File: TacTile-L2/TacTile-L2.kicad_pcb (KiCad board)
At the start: 2 copper layers, 21.2 x 60 mm, 11 parts, among them J1 Conn_01x05, J2 Conn_01x05, U1 74HC595

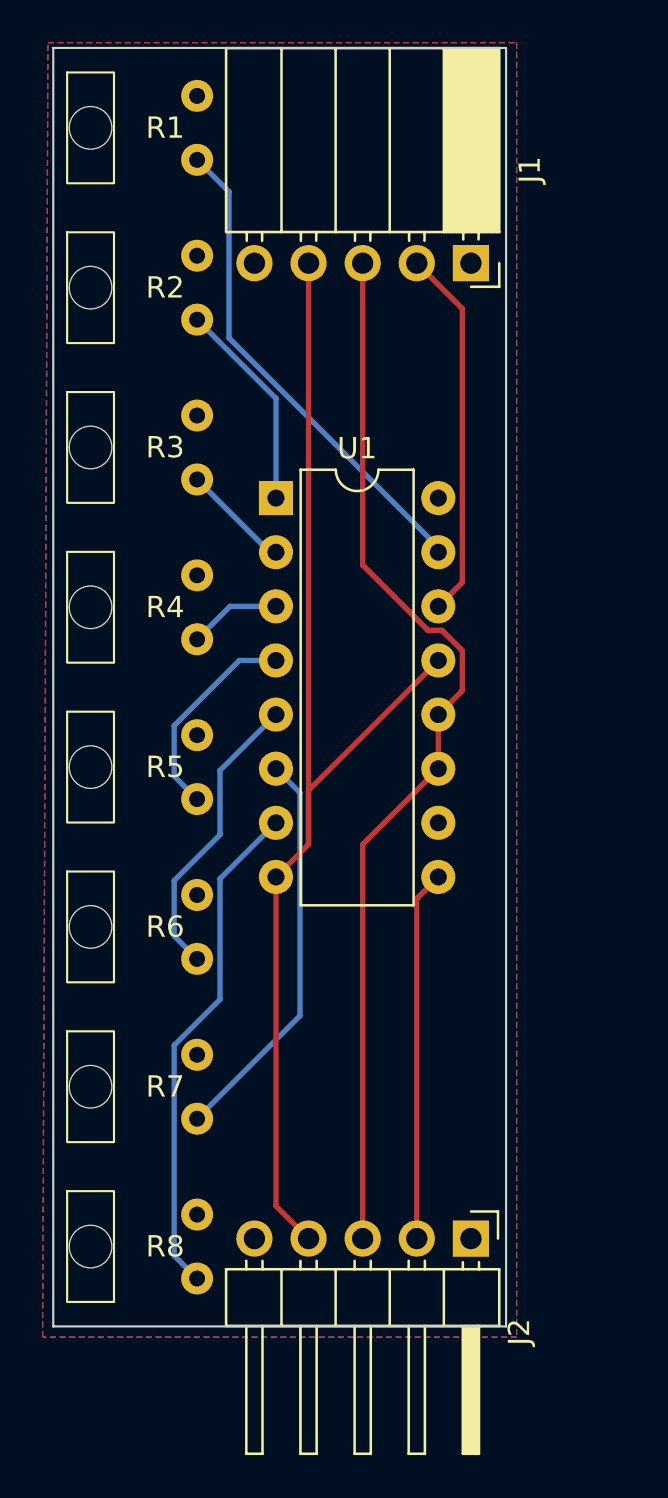
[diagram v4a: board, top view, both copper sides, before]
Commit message: Created connector boards for laser matrix
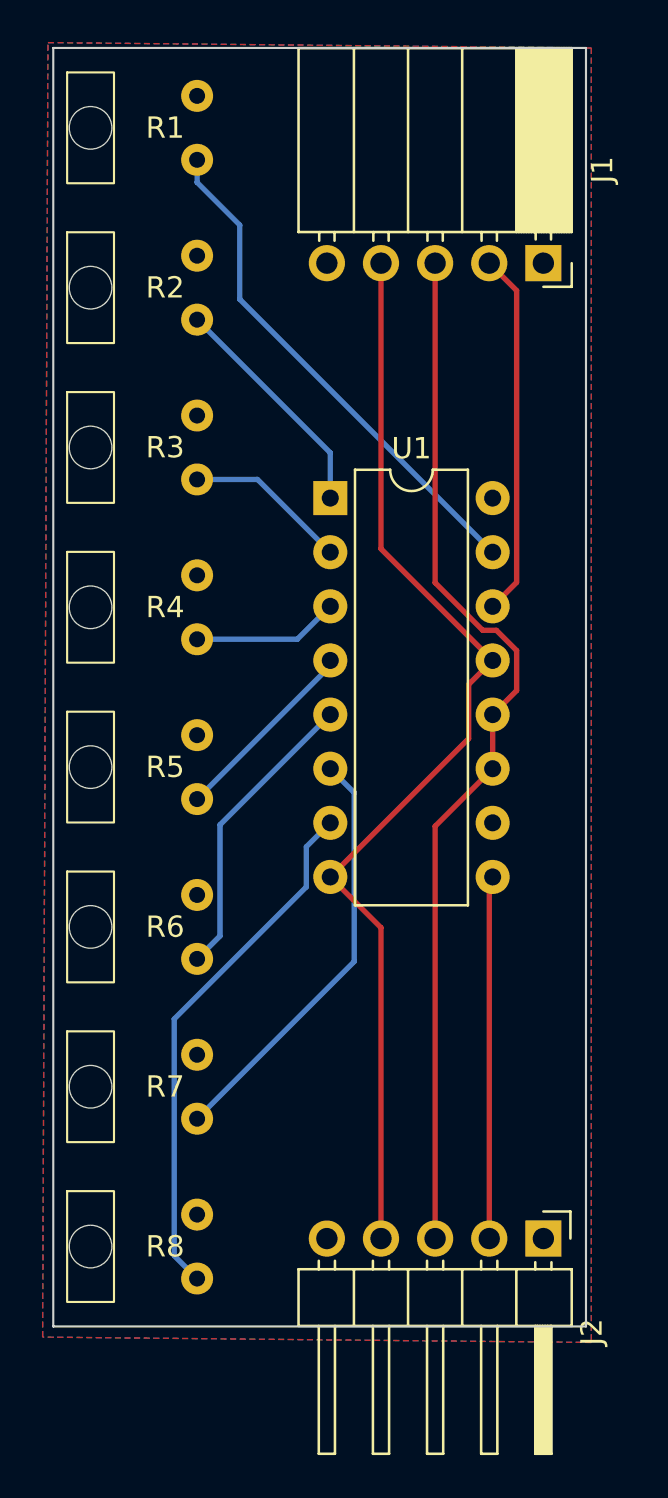
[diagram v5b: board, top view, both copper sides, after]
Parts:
- moved J1 3.40 mm to (48.0, 35.1)
- moved J2 3.40 mm to (48.0, 80.9)
- moved U1 2.55 mm to (38.0, 46.1)
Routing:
- net /GND: track 58.2 -> 52.1 mm
- net Net-(U1-QD): track 4.34 -> 6.89 mm
- net Net-(U1-QC): track 5.11 -> 7.66 mm
- net Net-(U1-QH): track 23.8 -> 24.9 mm
- net Net-(U1-QB): track 9.91 -> 11.0 mm
- net Net-(U1-QA): track 23.1 -> 24.2 mm
- net Net-(U1-QG): track 18.9 -> 19.9 mm
- net Net-(U1-QE): track 9.93 -> 9.09 mm
- net /CLK: track 50.0 -> 49.3 mm
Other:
- board size 21.2 x 60 mm -> 25 x 60 mm
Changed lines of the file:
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@@
   (net 14 "Net-(U1-QA)")
   (footprint "Connector_PinSocket_2.54mm:PinSocket_1x05_P2.54mm_Horizontal" (layer "F.Cu")
-    (at 44.6 35.1 -90)
+    (at 48 35.1 -90)
     (descr "Through hole angled socket strip, 1x05, 2.54mm pitch, 8.51mm socket length, single row (from Kicad 4.0.7), script generated")
     (tags "Through hole angled socket strip THT 1x05 2.54mm single row")
@@
   )
   (footprint "Package_DIP:DIP-16_W7.62mm" (layer "F.Cu")
-    (at 35.45 46.125)
+    (at 38 46.125)
     (descr "16-lead though-hole mounted DIP package, row spacing 7.62 mm (300 mils)")
     (tags "THT DIP DIL PDIP 2.54mm 7.62mm 300mil")
@@
   )
   (footprint "Connector_PinHeader_2.54mm:PinHeader_1x05_P2.54mm_Horizontal" (layer "F.Cu")
-    (at 44.6 80.875 -90)
+    (at 48 80.875 -90)
     (descr "Through hole angled pin header, 1x05, 2.54mm pitch, 6mm pin length, single row")
     (tags "Through hole angled pin header THT 1x05 2.54mm single row")
@@
     )
   )
-  (gr_rect (start 25 25) (end 46.25 85)
+  (gr_rect (start 25 25) (end 50 85)
     (stroke (width 0.1) (type default)) (fill none) (layer "Edge.Cuts"))
-  (segment (start 35.45 79.345) (end 36.98 80.875) (width 0.25) (layer "F.Cu") (net 2))
-  (segment (start 36.98 59.835) (end 36.98 62.375) (width 0.25) (layer "F.Cu") (net 2))
-  (segment (start 36.98 62.375) (end 35.45 63.905) (width 0.25) (layer "F.Cu") (net 2))
-  (segment (start 35.45 63.905) (end 35.45 79.345) (width 0.25) (layer "F.Cu") (net 2))
-  (segment (start 36.98 35.1) (end 36.98 62.375) (width 0.25) (layer "F.Cu") (net 2))
-  (segment (start 43.07 53.745) (end 36.98 59.835) (width 0.25) (layer "F.Cu") (net 2))
-  (segment (start 39.52 62.375) (end 39.52 80.875) (width 0.25) (layer "F.Cu") (net 3))
-  (segment (start 39.52 49.27) (end 39.52 35.1) (width 0.25) (layer "F.Cu") (net 3))
-  (segment (start 43.07 56.285) (end 43.07 58.825) (width 0.25) (layer "F.Cu") (net 3))
-  (segment (start 43.245991 52.33) (end 42.58 52.33) (width 0.25) (layer "F.Cu") (net 3))
-  (segment (start 44.195 53.279009) (end 43.245991 52.33) (width 0.25) (layer "F.Cu") (net 3))
-  (segment (start 42.58 52.33) (end 39.52 49.27) (width 0.25) (layer "F.Cu") (net 3))
-  (segment (start 43.07 56.285) (end 44.195 55.16) (width 0.25) (layer "F.Cu") (net 3))
-  (segment (start 43.07 58.825) (end 39.52 62.375) (width 0.25) (layer "F.Cu") (net 3))
-  (segment (start 44.195 55.16) (end 44.195 53.279009) (width 0.25) (layer "F.Cu") (net 3))
-  (segment (start 44.195 50.08) (end 43.07 51.205) (width 0.25) (layer "F.Cu") (net 4))
-  (segment (start 42.06 35.1) (end 44.195 37.235) (width 0.25) (layer "F.Cu") (net 4))
-  (segment (start 44.195 37.235) (end 44.195 50.08) (width 0.25) (layer "F.Cu") (net 4))
-  (segment (start 42.06 64.915) (end 43.07 63.905) (width 0.25) (layer "F.Cu") (net 6))
-  (segment (start 42.06 80.875) (end 42.06 64.915) (width 0.25) (layer "F.Cu") (net 6))
-  (segment (start 31.75 37.75) (end 35.45 41.45) (width 0.25) (layer "B.Cu") (net 7))
-  (segment (start 35.45 41.45) (end 35.45 46.125) (width 0.25) (layer "B.Cu") (net 7))
-  (segment (start 31.75 45.25) (end 35.165 48.665) (width 0.25) (layer "B.Cu") (net 8))
-  (segment (start 35.165 48.665) (end 35.45 48.665) (width 0.25) (layer "B.Cu") (net 8))
-  (segment (start 31.75 52.75) (end 33.295 51.205) (width 0.25) (layer "B.Cu") (net 9))
-  (segment (start 33.295 51.205) (end 35.45 51.205) (width 0.25) (layer "B.Cu") (net 9))
-  (segment (start 33.73472 53.745) (end 30.675 56.80472) (width 0.25) (layer "B.Cu") (net 10))
-  (segment (start 35.45 53.745) (end 33.73472 53.745) (width 0.25) (layer "B.Cu") (net 10))
-  (segment (start 30.675 59.175) (end 31.75 60.25) (width 0.25) (layer "B.Cu") (net 10))
-  (segment (start 30.675 56.80472) (end 30.675 59.175) (width 0.25) (layer "B.Cu") (net 10))
-  (segment (start 30.675 66.675) (end 31.75 67.75) (width 0.25) (layer "B.Cu") (net 11))
-  (segment (start 32.825 61.925) (end 30.675 64.075) (width 0.25) (layer "B.Cu") (net 11))
-  (segment (start 35.45 56.285) (end 32.825 58.91) (width 0.25) (layer "B.Cu") (net 11))
-  (segment (start 30.675 64.075) (end 30.675 66.675) (width 0.25) (layer "B.Cu") (net 11))
-  (segment (start 32.825 58.91) (end 32.825 61.925) (width 0.25) (layer "B.Cu") (net 11))
-  (segment (start 36.575 59.95) (end 35.45 58.825) (width 0.25) (layer "B.Cu") (net 12))
-  (segment (start 31.75 75.25) (end 36.575 70.425) (width 0.25) (layer "B.Cu") (net 12))
-  (segment (start 36.575 70.425) (end 36.575 59.95) (width 0.25) (layer "B.Cu") (net 12))
-  (segment (start 30.675 81.675) (end 31.75 82.75) (width 0.25) (layer "B.Cu") (net 13))
-  (segment (start 32.825 69.65472) (end 30.675 71.80472) (width 0.25) (layer "B.Cu") (net 13))
-  (segment (start 32.825 63.99) (end 32.825 69.65472) (width 0.25) (layer "B.Cu") (net 13))
-  (segment (start 35.45 61.365) (end 32.825 63.99) (width 0.25) (layer "B.Cu") (net 13))
-  (segment (start 30.675 71.80472) (end 30.675 81.675) (width 0.25) (layer "B.Cu") (net 13))
-  (segment (start 33.25 38.613604) (end 43.07 48.433604) (width 0.25) (layer "B.Cu") (net 14))
-  (segment (start 43.07 48.433604) (end 43.07 48.665) (width 0.25) (layer "B.Cu") (net 14))
-  (segment (start 31.75 30.25) (end 33.25 31.75) (width 0.25) (layer "B.Cu") (net 14))
-  (segment (start 33.25 31.75) (end 33.25 38.613604) (width 0.25) (layer "B.Cu") (net 14))
+  (segment (start 40.38 35.1) (end 40.38 48.505) (width 0.25) (layer "F.Cu") (net 2))
+  (segment (start 40.38 66.285) (end 38 63.905) (width 0.25) (layer "F.Cu") (net 2))
+  (segment (start 40.38 48.505) (end 45.62 53.745) (width 0.25) (layer "F.Cu") (net 2))
+  (segment (start 44.495 57.41) (end 44.495 54.87) (width 0.25) (layer "F.Cu") (net 2))
+  (segment (start 38 63.905) (end 44.495 57.41) (width 0.25) (layer "F.Cu") (net 2))
+  (segment (start 40.38 80.875) (end 40.38 66.285) (width 0.25) (layer "F.Cu") (net 2))
+  (segment (start 44.495 54.87) (end 45.62 53.745) (width 0.25) (layer "F.Cu") (net 2))
+  (segment (start 45.62 56.285) (end 45.62 58.825) (width 0.25) (layer "F.Cu") (net 3))
+  (segment (start 45.154009 52.33) (end 42.92 50.095991) (width 0.25) (layer "F.Cu") (net 3))
+  (segment (start 45.795991 52.33) (end 45.154009 52.33) (width 0.25) (layer "F.Cu") (net 3))
+  (segment (start 45.62 56.285) (end 46.745 55.16) (width 0.25) (layer "F.Cu") (net 3))
+  (segment (start 46.745 53.279009) (end 45.795991 52.33) (width 0.25) (layer "F.Cu") (net 3))
+  (segment (start 42.92 50.095991) (end 42.92 35.1) (width 0.25) (layer "F.Cu") (net 3))
+  (segment (start 42.92 61.525) (end 42.92 80.875) (width 0.25) (layer "F.Cu") (net 3))
+  (segment (start 45.62 58.825) (end 42.92 61.525) (width 0.25) (layer "F.Cu") (net 3))
+  (segment (start 46.745 55.16) (end 46.745 53.279009) (width 0.25) (layer "F.Cu") (net 3))
+  (segment (start 46.745 36.385) (end 46.745 50.08) (width 0.25) (layer "F.Cu") (net 4))
+  (segment (start 45.46 35.1) (end 46.745 36.385) (width 0.25) (layer "F.Cu") (net 4))
+  (segment (start 46.745 50.08) (end 45.62 51.205) (width 0.25) (layer "F.Cu") (net 4))
+  (segment (start 45.46 64.065) (end 45.62 63.905) (width 0.25) (layer "F.Cu") (net 6))
+  (segment (start 45.46 80.875) (end 45.46 64.065) (width 0.25) (layer "F.Cu") (net 6))
+  (segment (start 31.75 37.75) (end 38 44) (width 0.25) (layer "B.Cu") (net 7))
+  (segment (start 38 44) (end 38 46.125) (width 0.25) (layer "B.Cu") (net 7))
+  (segment (start 31.75 45.25) (end 34.585 45.25) (width 0.25) (layer "B.Cu") (net 8))
+  (segment (start 34.585 45.25) (end 38 48.665) (width 0.25) (layer "B.Cu") (net 8))
+  (segment (start 31.75 52.75) (end 36.455 52.75) (width 0.25) (layer "B.Cu") (net 9))
+  (segment (start 36.455 52.75) (end 38 51.205) (width 0.25) (layer "B.Cu") (net 9))
+  (segment (start 38 54) (end 38 53.745) (width 0.25) (layer "B.Cu") (net 10))
+  (segment (start 31.75 60.25) (end 38 54) (width 0.25) (layer "B.Cu") (net 10))
+  (segment (start 31.75 67.75) (end 32.825 66.675) (width 0.25) (layer "B.Cu") (net 11))
+  (segment (start 32.825 61.46) (end 38 56.285) (width 0.25) (layer "B.Cu") (net 11))
+  (segment (start 32.825 66.675) (end 32.825 61.46) (width 0.25) (layer "B.Cu") (net 11))
+  (segment (start 39.125 67.875) (end 39.125 59.95) (width 0.25) (layer "B.Cu") (net 12))
+  (segment (start 31.75 75.25) (end 39.125 67.875) (width 0.25) (layer "B.Cu") (net 12))
+  (segment (start 39.125 59.95) (end 38 58.825) (width 0.25) (layer "B.Cu") (net 12))
+  (segment (start 36.875 62.49) (end 38 61.365) (width 0.25) (layer "B.Cu") (net 13))
+  (segment (start 30.675 81.675) (end 30.675 70.575) (width 0.25) (layer "B.Cu") (net 13))
+  (segment (start 31.75 82.75) (end 30.675 81.675) (width 0.25) (layer "B.Cu") (net 13))
+  (segment (start 30.675 70.575) (end 36.875 64.375) (width 0.25) (layer "B.Cu") (net 13))
+  (segment (start 36.875 64.375) (end 36.875 62.49) (width 0.25) (layer "B.Cu") (net 13))
+  (segment (start 33.75 33.31066) (end 33.75 36.795) (width 0.25) (layer "B.Cu") (net 14))
+  (segment (start 33.75 36.795) (end 45.62 48.665) (width 0.25) (layer "B.Cu") (net 14))
+  (segment (start 31.75 30.25) (end 31.75 31.31066) (width 0.25) (layer "B.Cu") (net 14))
+  (segment (start 31.75 31.31066) (end 33.75 33.31066) (width 0.25) (layer "B.Cu") (net 14))
   (zone (net 5) (net_name "/OUT") (layer "F.Cu") (hatch edge 0.5)
     (connect_pads (clearance 0.5))
@@
       (pts
         (xy 24.75 24.75)
-        (xy 46.75 24.75)
-        (xy 46.75 85.5)
+        (xy 50.25 25)
+        (xy 50.25 85.75)
         (xy 24.5 85.5)
       )
@@
       (pts
         (xy 24.75 24.75)
-        (xy 46.75 24.75)
-        (xy 46.75 85.5)
+        (xy 50.25 25)
+        (xy 50.25 85.75)
         (xy 24.5 85.5)
       )
